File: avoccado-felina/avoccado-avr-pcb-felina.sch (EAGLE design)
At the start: 60 parts, among them Q1 16MHz, Q2 FET, U2 MCP73831

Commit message: Faye: adjusted Rs, new PCB: Felina
Felina is a larger PCB with the MPU6050 on board instead of a breakout
board.
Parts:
- added C11, C8: 0.1uF, SparkFun:CAP0402
- added C9: 2.2nF, SparkFun:CAP0402
- added R10, R11: 10K, SparkFun-Resistors:RESISTOR0603
- added U1: MPU-6000QFN-24, SparkFun-Sensors:MPU-6000QFN-24
- C1, C3: device SparkFun:CAP0402 -> resistor:C-EUC0402K
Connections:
- removed net D2: MCU.PD2(INT0), TP2.1
- new net D2-INT: MCU.PD2(INT0), TP2.1, U1.INT
- new net N$10: C11.1, U1.CS
- new net N$4: R10.1, U1.SCL/SCLK
- new net N$5: R11.1, U1.SDA/SDI
- new net N$7: C8.1, U1.REGOUT
- new net N$8: C9.1, U1.CPOUT
- net 3.3V: now also R10.2, R11.2, U1.VDD
- net GND: now also C11.2, C8.2, C9.2, U1.AD0/SDO, U1.CLKIN, U1.FSYNC, U1.GND
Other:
- moved on the sheet: C1, C3
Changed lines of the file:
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@@
 <part name="GND26" library="SparkFun" deviceset="GND" device=""/>
 <part name="R2" library="SparkFun-Resistors" deviceset="RESISTOR" device="0603" value="10K"/>
-<part name="C3" library="SparkFun" deviceset="CAP" device="0402" value="0.1uF"/>
+<part name="C3" library="resistor" deviceset="C-EU" device="C0402K" value="0.1uF"/>
 <part name="GND1" library="SparkFun" deviceset="GND" device=""/>
-<part name="C1" library="SparkFun" deviceset="CAP" device="0402" value="0.1uF"/>
+<part name="C1" library="resistor" deviceset="C-EU" device="C0402K" value="0.1uF"/>
 <part name="GND7" library="SparkFun" deviceset="GND" device=""/>
 <part name="GND30" library="SparkFun" deviceset="GND" device=""/>
@@
 <part name="TP4" library="SparkFun-Passives" deviceset="TEST-POINT" device="3"/>
 <part name="TP9" library="SparkFun-Passives" deviceset="TEST-POINT" device="2"/>
+<part name="U1" library="SparkFun-Sensors" deviceset="MPU-6000" device="QFN-24"/>
+<part name="R10" library="SparkFun-Resistors" deviceset="RESISTOR" device="0603" value="10K"/>
+<part name="R11" library="SparkFun-Resistors" deviceset="RESISTOR" device="0603" value="10K"/>
+<part name="P+2" library="SparkFun" deviceset="3.3V" device="" value="3V3"/>
+<part name="GND11" library="SparkFun" deviceset="GND" device=""/>
+<part name="GND12" library="SparkFun" deviceset="GND" device=""/>
+<part name="P+3" library="SparkFun" deviceset="3.3V" device="" value="3V3"/>
+<part name="C8" library="SparkFun" deviceset="CAP" device="0402" value="0.1uF"/>
+<part name="GND13" library="SparkFun" deviceset="GND" device=""/>
+<part name="C9" library="SparkFun" deviceset="CAP" device="0402" value="2.2nF"/>
+<part name="C11" library="SparkFun" deviceset="CAP" device="0402" value="0.1uF"/>
+<part name="GND14" library="SparkFun" deviceset="GND" device=""/>
+<part name="GND15" library="SparkFun" deviceset="GND" device=""/>
+<part name="P+4" library="SparkFun" deviceset="3.3V" device="" value="3V3"/>
 </parts>
 <sheets>
@@
 <instance part="TP4" gate="G$1" x="18.288" y="177.8" rot="R180"/>
 <instance part="TP9" gate="G$1" x="276.86" y="139.7"/>
+<instance part="U1" gate="G$1" x="-73.66" y="137.16"/>
+<instance part="R10" gate="G$1" x="-38.1" y="154.94" rot="R90"/>
+<instance part="R11" gate="G$1" x="-25.4" y="154.94" rot="R90"/>
+<instance part="P+2" gate="G$1" x="-38.1" y="165.1"/>
+<instance part="GND11" gate="1" x="-33.02" y="106.68"/>
+<instance part="GND12" gate="1" x="-109.22" y="106.68"/>
+<instance part="P+3" gate="G$1" x="-99.06" y="165.1"/>
+<instance part="C8" gate="G$1" x="-137.16" y="127"/>
+<instance part="GND13" gate="1" x="-137.16" y="106.68"/>
+<instance part="C9" gate="G$1" x="-121.92" y="127"/>
+<instance part="C11" gate="G$1" x="-43.18" y="127"/>
+<instance part="GND14" gate="1" x="-121.92" y="106.68"/>
+<instance part="GND15" gate="1" x="-43.18" y="106.68"/>
+<instance part="P+4" gate="G$1" x="-25.4" y="165.1"/>
 </instances>
 <busses>
@@
 </segment>
 <segment>
-<wire x1="154.94" y1="96.52" x2="154.94" y2="99.06" width="0.1524" layer="91"/>
+<wire x1="154.94" y1="96.52" x2="154.94" y2="101.6" width="0.1524" layer="91"/>
 <pinref part="C3" gate="G$1" pin="1"/>
 <pinref part="GND1" gate="1" pin="GND"/>
 </segment>
 <segment>
-<wire x1="149.86" y1="127" x2="149.86" y2="129.54" width="0.1524" layer="91"/>
+<wire x1="149.86" y1="127" x2="149.86" y2="132.08" width="0.1524" layer="91"/>
 <pinref part="C1" gate="G$1" pin="1"/>
 <pinref part="GND7" gate="1" pin="GND"/>
@@
 <pinref part="TP9" gate="G$1" pin="1"/>
 </segment>
+<segment>
+<pinref part="U1" gate="G$1" pin="AD0/SDO"/>
+<pinref part="GND11" gate="1" pin="GND"/>
+<wire x1="-55.88" y1="139.7" x2="-33.02" y2="139.7" width="0.1524" layer="91"/>
+<wire x1="-33.02" y1="139.7" x2="-33.02" y2="109.22" width="0.1524" layer="91"/>
+</segment>
+<segment>
+<pinref part="U1" gate="G$1" pin="CLKIN"/>
+<pinref part="GND12" gate="1" pin="GND"/>
+<wire x1="-91.44" y1="137.16" x2="-109.22" y2="137.16" width="0.1524" layer="91"/>
+<wire x1="-109.22" y1="137.16" x2="-109.22" y2="129.54" width="0.1524" layer="91"/>
+<pinref part="U1" gate="G$1" pin="FSYNC"/>
+<wire x1="-109.22" y1="129.54" x2="-109.22" y2="109.22" width="0.1524" layer="91"/>
+<wire x1="-91.44" y1="139.7" x2="-109.22" y2="139.7" width="0.1524" layer="91"/>
+<wire x1="-109.22" y1="139.7" x2="-109.22" y2="137.16" width="0.1524" layer="91"/>
+<junction x="-109.22" y="137.16"/>
+<pinref part="U1" gate="G$1" pin="GND"/>
+<wire x1="-91.44" y1="129.54" x2="-109.22" y2="129.54" width="0.1524" layer="91"/>
+<junction x="-109.22" y="129.54"/>
+</segment>
+<segment>
+<pinref part="C8" gate="G$1" pin="2"/>
+<pinref part="GND13" gate="1" pin="GND"/>
+<wire x1="-137.16" y1="124.46" x2="-137.16" y2="109.22" width="0.1524" layer="91"/>
+</segment>
+<segment>
+<pinref part="C9" gate="G$1" pin="2"/>
+<pinref part="GND14" gate="1" pin="GND"/>
+<wire x1="-121.92" y1="124.46" x2="-121.92" y2="109.22" width="0.1524" layer="91"/>
+</segment>
+<segment>
+<pinref part="C11" gate="G$1" pin="2"/>
+<pinref part="GND15" gate="1" pin="GND"/>
+<wire x1="-43.18" y1="124.46" x2="-43.18" y2="109.22" width="0.1524" layer="91"/>
+</segment>
 </net>
 <net name="AREF" class="0">
 <segment>
 <wire x1="167.64" y1="139.7" x2="149.86" y2="139.7" width="0.1524" layer="91"/>
-<wire x1="149.86" y1="139.7" x2="149.86" y2="137.16" width="0.1524" layer="91"/>
 <label x="157.48" y="139.7" size="1.778" layer="95"/>
 <pinref part="C1" gate="G$1" pin="2"/>
@@
 </segment>
 <segment>
-<wire x1="154.94" y1="109.22" x2="154.94" y2="106.68" width="0.1524" layer="91"/>
 <pinref part="C3" gate="G$1" pin="2"/>
 <pinref part="P+15" gate="G$1" pin="3.3V"/>
@@
 <label x="101.6" y="33.02" size="1.778" layer="95"/>
 </segment>
+<segment>
+<pinref part="U1" gate="G$1" pin="VDD"/>
+<pinref part="P+3" gate="G$1" pin="3.3V"/>
+<wire x1="-91.44" y1="144.78" x2="-99.06" y2="144.78" width="0.1524" layer="91"/>
+<wire x1="-99.06" y1="144.78" x2="-99.06" y2="165.1" width="0.1524" layer="91"/>
+</segment>
+<segment>
+<pinref part="R10" gate="G$1" pin="2"/>
+<wire x1="-38.1" y1="160.02" x2="-38.1" y2="165.1" width="0.1524" layer="91"/>
+<pinref part="P+2" gate="G$1" pin="3.3V"/>
+</segment>
+<segment>
+<pinref part="R11" gate="G$1" pin="2"/>
+<wire x1="-25.4" y1="160.02" x2="-25.4" y2="165.1" width="0.1524" layer="91"/>
+<pinref part="P+4" gate="G$1" pin="3.3V"/>
+</segment>
 </net>
 <net name="D9" class="0">
@@
 </segment>
 </net>
-<net name="D2" class="0">
+<net name="D2-INT" class="0">
 <segment>
 <wire x1="215.9" y1="127" x2="226.06" y2="127" width="0.1524" layer="91"/>
@@
 <pinref part="TP2" gate="G$1" pin="1"/>
 <label x="106.68" y="7.62" size="1.778" layer="95"/>
+</segment>
+<segment>
+<wire x1="-119.38" y1="142.24" x2="-91.44" y2="142.24" width="0.1524" layer="91"/>
+<pinref part="U1" gate="G$1" pin="INT"/>
+<label x="-119.38" y="142.24" size="1.778" layer="95"/>
 </segment>
 </net>
@@
 </segment>
 </net>
+<net name="N$4" class="0">
+<segment>
+<pinref part="U1" gate="G$1" pin="SCL/SCLK"/>
+<pinref part="R10" gate="G$1" pin="1"/>
+<wire x1="-55.88" y1="142.24" x2="-38.1" y2="142.24" width="0.1524" layer="91"/>
+<wire x1="-38.1" y1="142.24" x2="-38.1" y2="149.86" width="0.1524" layer="91"/>
+</segment>
+</net>
+<net name="N$5" class="0">
+<segment>
+<pinref part="U1" gate="G$1" pin="SDA/SDI"/>
+<pinref part="R11" gate="G$1" pin="1"/>
+<wire x1="-55.88" y1="137.16" x2="-25.4" y2="137.16" width="0.1524" layer="91"/>
+<wire x1="-25.4" y1="137.16" x2="-25.4" y2="149.86" width="0.1524" layer="91"/>
+</segment>
+</net>
+<net name="N$7" class="0">
+<segment>
+<pinref part="U1" gate="G$1" pin="REGOUT"/>
+<pinref part="C8" gate="G$1" pin="1"/>
+<wire x1="-91.44" y1="134.62" x2="-137.16" y2="134.62" width="0.1524" layer="91"/>
+<wire x1="-137.16" y1="134.62" x2="-137.16" y2="132.08" width="0.1524" layer="91"/>
+</segment>
+</net>
+<net name="N$8" class="0">
+<segment>
+<pinref part="U1" gate="G$1" pin="CPOUT"/>
+<pinref part="C9" gate="G$1" pin="1"/>
+<wire x1="-91.44" y1="132.08" x2="-121.92" y2="132.08" width="0.1524" layer="91"/>
+</segment>
+</net>
+<net name="N$10" class="0">
+<segment>
+<pinref part="U1" gate="G$1" pin="CS"/>
+<pinref part="C11" gate="G$1" pin="1"/>
+<wire x1="-55.88" y1="144.78" x2="-43.18" y2="144.78" width="0.1524" layer="91"/>
+<wire x1="-43.18" y1="144.78" x2="-43.18" y2="132.08" width="0.1524" layer="91"/>
+</segment>
+</net>

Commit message: Felina: rearrange and start to route
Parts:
- JP12: value M01PTH -> M01NOSILK-KIT; device SparkFun-Connectors:M01PTH -> SparkFun-Connectors:M01NOSILK-KIT
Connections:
- removed net N$4: R10.1, U1.SCL/SCLK
- removed net N$5: R11.1, U1.SDA/SDI
- net A4: now also R11.1, U1.SDA/SDI
- net A5: now also R10.1, U1.SCL/SCLK
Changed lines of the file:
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@@
 <part name="JP10" library="SparkFun-Connectors" deviceset="M01" device="PTH" value="M01PTH"/>
 <part name="JP11" library="SparkFun-Connectors" deviceset="M01" device="PTH" value="M01PTH"/>
-<part name="JP12" library="SparkFun-Connectors" deviceset="M01" device="PTH" value="M01PTH"/>
+<part name="JP12" library="SparkFun-Connectors" deviceset="M01" device="NOSILK-KIT" value="M01NOSILK-KIT"/>
 <part name="JP13" library="SparkFun-Connectors" deviceset="M01" device="PTH" value="M01PTH"/>
 <part name="JP14" library="SparkFun-Connectors" deviceset="M01" device="NOSILK-KIT" value="M01NOSILK-KIT"/>
@@
 <label x="101.6" y="27.94" size="1.778" layer="95"/>
 </segment>
+<segment>
+<wire x1="-53.34" y1="147.32" x2="-38.1" y2="147.32" width="0.1524" layer="91"/>
+<pinref part="U1" gate="G$1" pin="SCL/SCLK"/>
+<pinref part="R10" gate="G$1" pin="1"/>
+<wire x1="-55.88" y1="142.24" x2="-38.1" y2="142.24" width="0.1524" layer="91"/>
+<wire x1="-38.1" y1="142.24" x2="-38.1" y2="147.32" width="0.1524" layer="91"/>
+<wire x1="-38.1" y1="147.32" x2="-38.1" y2="149.86" width="0.1524" layer="91"/>
+<junction x="-38.1" y="147.32"/>
+</segment>
 </net>
 <net name="A4" class="0">
@@
 <pinref part="JP5" gate="G$1" pin="2"/>
 <label x="101.6" y="25.4" size="1.778" layer="95"/>
+</segment>
+<segment>
+<wire x1="-25.4" y1="137.16" x2="-5.08" y2="137.16" width="0.1524" layer="91"/>
+<pinref part="U1" gate="G$1" pin="SDA/SDI"/>
+<pinref part="R11" gate="G$1" pin="1"/>
+<wire x1="-55.88" y1="137.16" x2="-25.4" y2="137.16" width="0.1524" layer="91"/>
+<wire x1="-25.4" y1="137.16" x2="-25.4" y2="149.86" width="0.1524" layer="91"/>
+<junction x="-25.4" y="137.16"/>
 </segment>
 </net>
@@
 </segment>
 </net>
-<net name="N$4" class="0">
-<segment>
-<pinref part="U1" gate="G$1" pin="SCL/SCLK"/>
-<pinref part="R10" gate="G$1" pin="1"/>
-<wire x1="-55.88" y1="142.24" x2="-38.1" y2="142.24" width="0.1524" layer="91"/>
-<wire x1="-38.1" y1="142.24" x2="-38.1" y2="149.86" width="0.1524" layer="91"/>
-</segment>
-</net>
-<net name="N$5" class="0">
-<segment>
-<pinref part="U1" gate="G$1" pin="SDA/SDI"/>
-<pinref part="R11" gate="G$1" pin="1"/>
-<wire x1="-55.88" y1="137.16" x2="-25.4" y2="137.16" width="0.1524" layer="91"/>
-<wire x1="-25.4" y1="137.16" x2="-25.4" y2="149.86" width="0.1524" layer="91"/>
-</segment>
-</net>

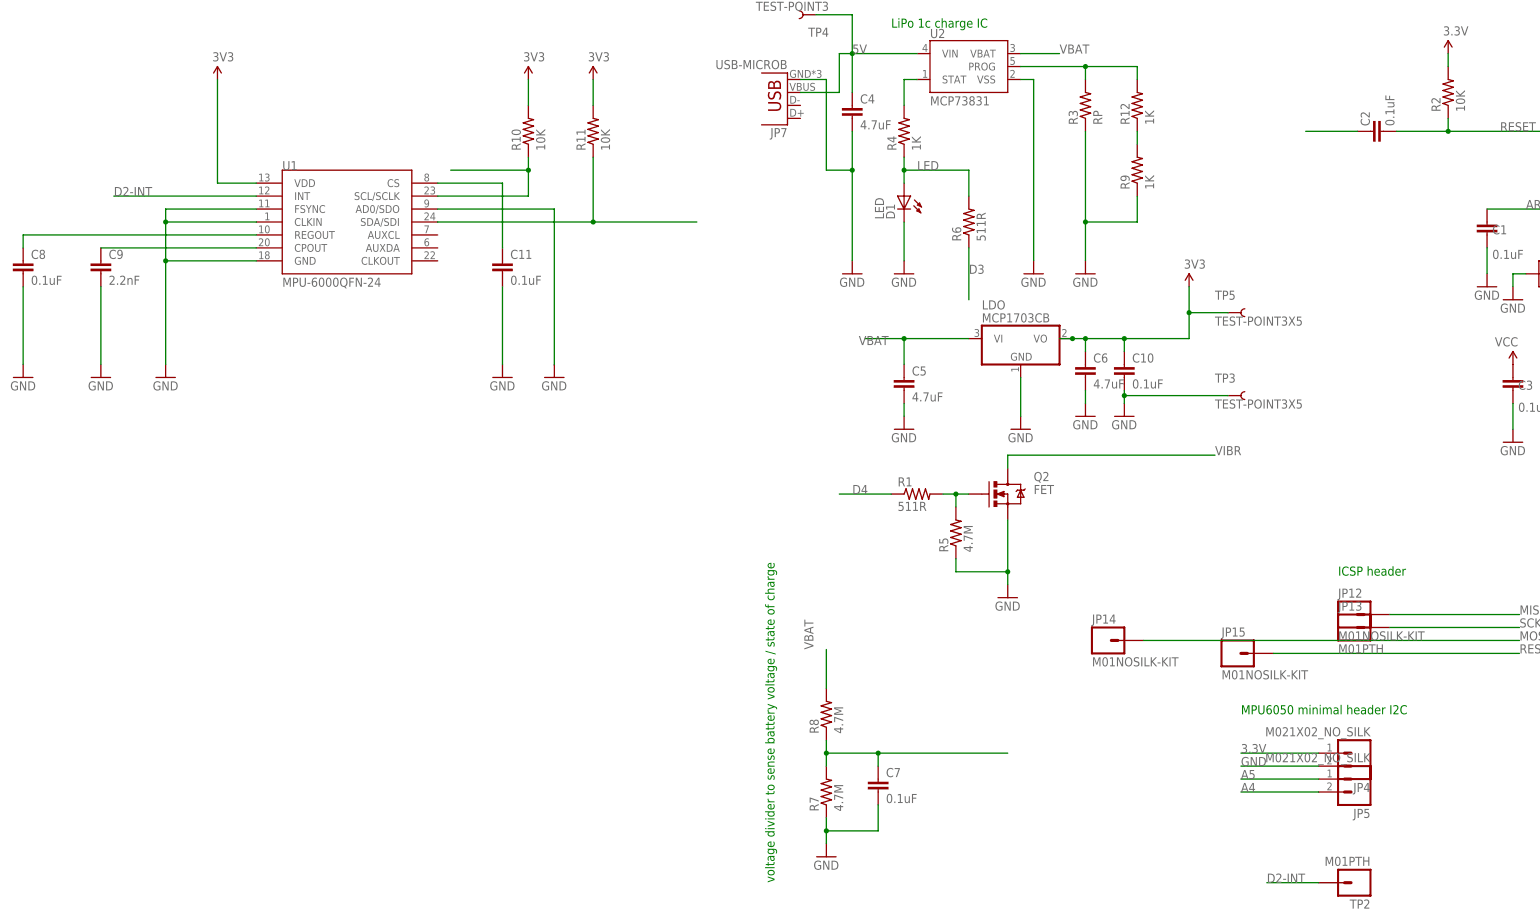
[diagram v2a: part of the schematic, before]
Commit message: move RST pullup away from bottom left
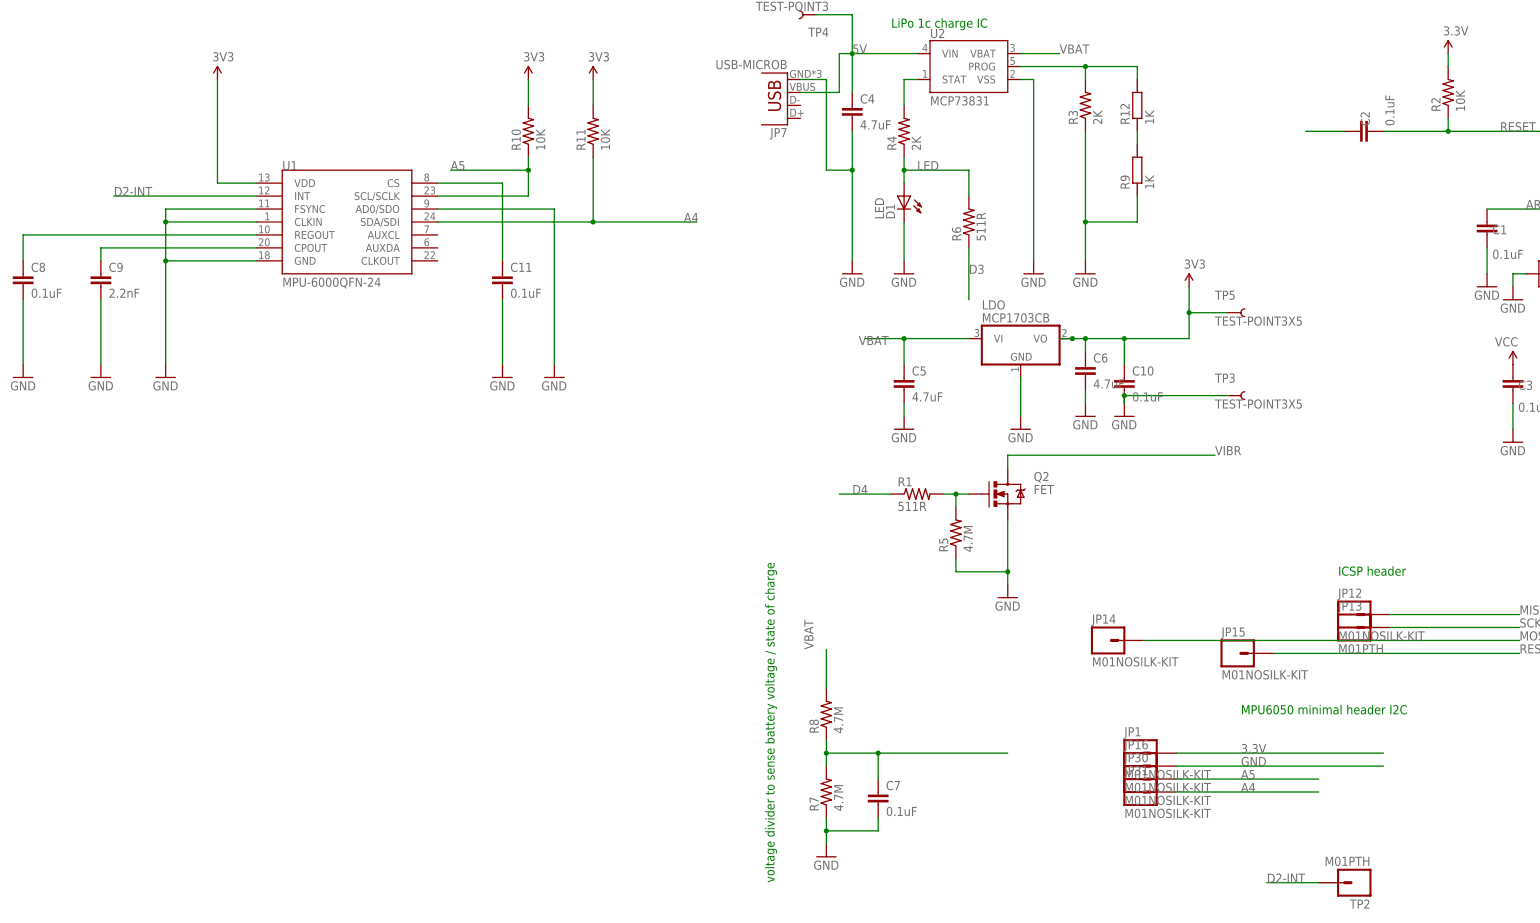
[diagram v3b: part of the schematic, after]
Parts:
- removed JP4, JP5: M021X02_NO_SILK, SparkFun-Connectors:M021X02_NO_SILK
- added JP1, JP16, JP30, JP31: M01NOSILK-KIT, SparkFun-Connectors:M01NOSILK-KIT
- C10, C11, C2, C7, C8, C9: device SparkFun:CAP0402 -> rcl:C-EUC0402K
- R12, R9: device SparkFun-Resistors:RESISTOR0402 -> rcl:R-EU_R0402
- R3: value RP -> 2K
- R4: value 1K -> 2K
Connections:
- net 3.3V: now also JP1.1; no longer JP4.1
- net A4: now also JP31.1; no longer JP5.2
- net A5: now also JP30.1; no longer JP5.1
- net GND: now also JP16.1; no longer JP4.2
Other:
- moved on the sheet: C10, C11, C2, C7, C8, C9
